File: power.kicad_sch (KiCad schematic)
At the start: 0 parts

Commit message: finish
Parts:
- added C26: 1uF, symbol G-Love:C
- added C27: 100nF, symbol G-Love:C
- added R16: 10K, symbol G-Love:R
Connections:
- new net +5V: C26.1, C27.1, R16.2
- new net GND: C26.2, C27.2, R16.1

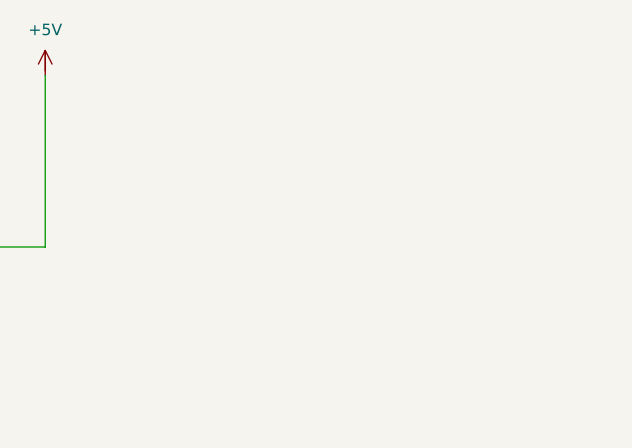
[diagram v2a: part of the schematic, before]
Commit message: Je crois que j'ai fini, je fais l'erc demain en revoyant la logique des switch, notamment les selections avec transistors
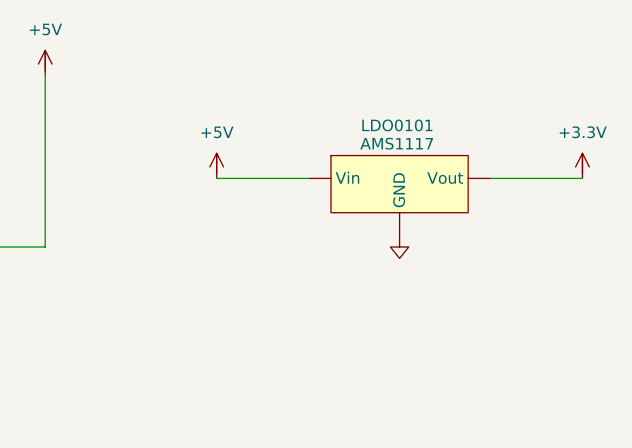
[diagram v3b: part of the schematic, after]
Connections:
- net GND is gone; now on net +5V: C26.2, C27.2, R16.1

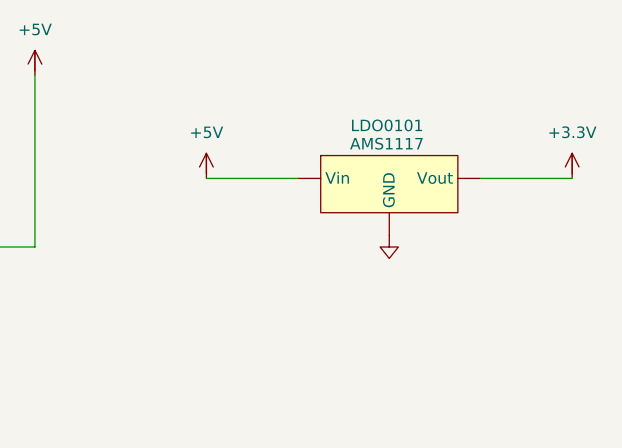
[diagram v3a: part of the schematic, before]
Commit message: To Do : Finir les condo pour chaque broche d'alimentation au moins avec ERC
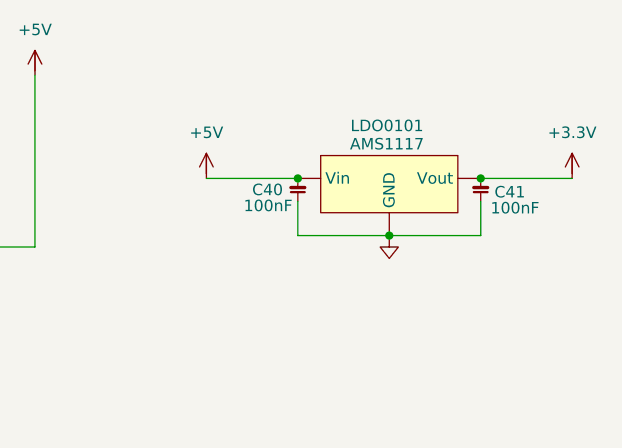
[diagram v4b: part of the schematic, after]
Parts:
- added C40, C41: 100nF, symbol G-Love:C
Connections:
- net +3.3V: now also C41.1
- net +5V: now also C40.1, C40.2, C41.2
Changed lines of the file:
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@@
+	)
+	(junction
+		(at 156.21 62.23)
+		(diameter 0)
+		(color 0 0 0 0)
+	)
+	(junction
+		(at 146.05 55.88)
+		(diameter 0)
+		(color 0 0 0 0)
+	)
+	(junction
+		(at 166.37 55.88)
+		(diameter 0)
+		(color 0 0 0 0)
 	)
 	(junction
@@
 	(wire
 		(pts
-			(xy 176.53 55.88) (xy 166.37 55.88)
+			(xy 146.05 62.23) (xy 156.21 62.23)
+		)
+		(stroke
+			(width 0)
+			(type default)
+		)
+	)
+	(wire
+		(pts
+			(xy 166.37 58.42) (xy 166.37 62.23)
 		)
 		(stroke
@@
 	(wire
 		(pts
+			(xy 166.37 55.88) (xy 176.53 55.88)
+		)
+		(stroke
+			(width 0)
+			(type default)
+		)
+	)
+	(wire
+		(pts
+			(xy 166.37 62.23) (xy 156.21 62.23)
+		)
+		(stroke
+			(width 0)
+			(type default)
+		)
+	)
+	(wire
+		(pts
 			(xy 67.31 63.5) (xy 76.2 63.5)
+		)
+		(stroke
+			(width 0)
+			(type default)
+		)
+	)
+	(wire
+		(pts
+			(xy 146.05 58.42) (xy 146.05 62.23)
 		)
 		(stroke
@@
 	(symbol
 		(lib_id "G-Love:C")
+		(at 146.05 57.15 0)
+		(unit 1)
+		(body_style 1)
+		(exclude_from_sim no)
+		(in_bom yes)
+		(on_board yes)
+		(in_pos_files yes)
+		(dnp no)
+		(property "Reference" "C40"
+			(at 140.97 57.15 0)
+			(show_name no)
+			(do_not_autoplace no)
+			(effects
+				(font
+					(size 1.27 1.27)
+				)
+				(justify left)
+			)
+		)
+		(property "Value" "100nF"
+			(at 142.748 58.928 0)
+			(show_name no)
+			(do_not_autoplace no)
+			(effects
+				(font
+					(size 1.27 1.27)
+				)
+			)
+		)
+		(property "Footprint" ""
+			(at 146.05 57.15 0)
+			(hide yes)
+			(show_name no)
+			(do_not_autoplace no)
+			(effects
+				(font
+					(size 1.27 1.27)
+				)
+			)
+		)
+		(property "Datasheet" ""
+			(at 146.05 57.15 0)
+			(hide yes)
+			(show_name no)
+			(do_not_autoplace no)
+			(effects
+				(font
+					(size 1.27 1.27)
+				)
+			)
+		)
+		(property "Description" "Capacitor"
+			(at 146.05 66.294 0)
+			(hide yes)
+			(show_name no)
+			(do_not_autoplace no)
+			(effects
+				(font
+					(size 1.27 1.27)
+				)
+			)
+		)
+		(pin "2"
+		)
+		(pin "1"
+		)
+		(instances
+			(project "G-Love"
+				(path "/808bc5ea-49ac-4454-ba77-8b20d01ce159/7d8a1e93-5494-4471-871c-2c3abe915f88"
+					(reference "C40")
+					(unit 1)
+				)
+			)
+		)
+	)
+	(symbol
+		(lib_id "G-Love:C")
 		(at 76.2 68.58 0)
 		(unit 1)
@@
 					(unit 1)
 				)
+			)
+		)
+	)
+	(symbol
+		(lib_id "G-Love:C")
+		(at 166.37 57.15 0)
+		(unit 1)
+		(body_style 1)
+		(exclude_from_sim no)
+		(in_bom yes)
+		(on_board yes)
+		(in_pos_files yes)
+		(dnp no)
+		(property "Reference" "C41"
+			(at 167.894 57.404 0)
+			(show_name no)
+			(do_not_autoplace no)
+			(effects
+				(font
+					(size 1.27 1.27)
+				)
+				(justify left)
+			)
+		)
+		(property "Value" "100nF"
+			(at 170.18 59.182 0)
+			(show_name no)
+			(do_not_autoplace no)
+			(effects
+				(font
+					(size 1.27 1.27)
+				)
+			)
+		)
+		(property "Footprint" ""
+			(at 166.37 57.15 0)
+			(hide yes)
+			(show_name no)
+			(do_not_autoplace no)
+			(effects
+				(font
+					(size 1.27 1.27)
+				)
+			)
+		)
+		(property "Datasheet" ""
+			(at 166.37 57.15 0)
+			(hide yes)
+			(show_name no)
+			(do_not_autoplace no)
+			(effects
+				(font
+					(size 1.27 1.27)
+				)
+			)
+		)
+		(property "Description" "Capacitor"
+			(at 166.37 66.294 0)
+			(hide yes)
+			(show_name no)
+			(do_not_autoplace no)
+			(effects
+				(font
+					(size 1.27 1.27)
+				)
+			)
+		)
+		(pin "1"
+		)
+		(pin "2"
+		)
+		(instances
+			(project "G-Love"
+				(path "/808bc5ea-49ac-4454-ba77-8b20d01ce159/7d8a1e93-5494-4471-871c-2c3abe915f88"
+					(reference "C41")
+					(unit 1)
+				)

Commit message: version final V1
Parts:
- added C29, C47: 1uF, symbol G-Love:C
- added C48: 4.7uF, symbol Device:C_Polarized_Small_US
- added C53: 10uF, symbol G-Love:C
- added R29: 560R, symbol G-Love:R
- added R32: 47k, symbol G-Love:R
- added R34: 10k, symbol G-Love:R
- added U14: TPS2113APWR, TPS2113APWR:SOP65P640X120-8N, symbol G-Love:TPS2113APWR
- renumbered C26 to C28, C27 to C31, C40 to C49, C41 to C50, R16 to R31
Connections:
- net +3.3V: now also C53.1
- net +5V: now also C29.1, C47.1, C48.1, C48.2, C53.2, R29.1, R34.1, U14.2 (~{EN}), U14.5 (GND), U14.7 (OUT)
- new net: R32.2, U14.3 (VSNS)
- new net: R29.2, U14.4 (ILIM)
- new net BATTERY_USB: C47.2, U14.6 (IN2)
- new net PC_USB: C29.2, R32.1, R34.2, U14.8 (IN1)
- no-connect marks 0 -> 1
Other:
- note added: "Alimentation LEDs"
- note added: "Alimentation PCB"
- note added: "LDO Sortie 3.3V"
- note added: "Pont diviseur de tension: si PC_USB < 4.3V, VSNS < 0.8V switch d'alim sur batterie Sinon utilisation USB"
- moved on the sheet: C28, C31, C49, C50, R31

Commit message: add: bom
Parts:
- C28, C29, C47: Price (none) -> 4.39/50; SUPPLIER (none) -> https://www.lcsc.com/product-detail/C15849.html
- C31, C49, C50: Price (none) -> 1.44/100; SUPPLIER (none) -> https://www.lcsc.com/product-detail/C1591.html
- C48: Price (none) -> 0.33/10; SUPPLIER (none) -> https://www.lcsc.com/product-detail/C19666.html
- C53: Price (none) -> 2.17/20; SUPPLIER (none) -> https://www.lcsc.com/product-detail/C15850.html
- R29: Price (none) -> 0.63/100; SUPPLIER (none) -> https://www.lcsc.com/product-detail/C23204.html
- R31: value 10K -> 10kΩ; Price (none) -> 0.74/100; SUPPLIER (none) -> https://www.lcsc.com/product-detail/C844918.html
- R32: Price (none) -> 0.24/100; SUPPLIER (none) -> https://www.lcsc.com/product-detail/C2907042.html
- R34: value 10k -> 10kΩ; Price (none) -> 0.74/100; SUPPLIER (none) -> https://www.lcsc.com/product-detail/C844918.html
- U14: Price None -> 2.67; SUPPLIER (none) -> https://www.lcsc.com/product-detail/C130052.html

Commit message: finished all footprints + redid some symbols, ready for PCB
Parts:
- C28, C29, C31, C47, C49, C50, C53: footprint (none) -> G-Love:Capacitor_0603
- C48: footprint (none) -> G-Love:Capacitor_Electrolytic
- R29, R31, R32, R34: footprint (none) -> G-Love:Resistor_0603
- U14: footprint TPS2113APWR:SOP65P640X120-8N -> G-Love:TPS2113
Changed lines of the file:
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@@
 			)
 		)
-		(property "Footprint" ""
+		(property "Footprint" "G-Love:Capacitor_0603"
 			(at 53.34 64.77 0)
 			(hide yes)
@@
 			)
 		)
-		(property "Footprint" "TPS2113APWR:SOP65P640X120-8N"
+		(property "Footprint" "G-Love:TPS2113"
 			(at 69.85 158.75 0)
 			(hide yes)
@@
 			)
 		)
-		(property "Footprint" ""
+		(property "Footprint" "G-Love:Capacitor_0603"
 			(at 142.24 154.94 0)
 			(hide yes)
@@
 			)
 		)
-		(property "Footprint" ""
+		(property "Footprint" "G-Love:Capacitor_0603"
 			(at 50.8 163.83 0)
 			(hide yes)
@@
 			)
 		)
-		(property "Footprint" ""
+		(property "Footprint" "G-Love:Capacitor_Electrolytic"
 			(at 91.44 160.02 0)
 			(hide yes)
@@
 			)
 		)
-		(property "Footprint" ""
+		(property "Footprint" "G-Love:Resistor_0603"
 			(at 66.04 64.77 0)
 			(hide yes)
@@
 			)
 		)
-		(property "Footprint" ""
+		(property "Footprint" "G-Love:Resistor_0603"
 			(at 44.45 153.67 0)
 			(hide yes)
@@
 			)
 		)
-		(property "Footprint" ""
+		(property "Footprint" "G-Love:Capacitor_0603"
 			(at 120.65 157.48 0)
 			(hide yes)
@@
 			)
 		)
-		(property "Footprint" ""
+		(property "Footprint" "G-Love:Capacitor_0603"
 			(at 40.64 64.77 0)
 			(hide yes)
@@
 			)
 		)
-		(property "Footprint" ""
+		(property "Footprint" "G-Love:Resistor_0603"
 			(at 87.63 146.05 0)
 			(hide yes)
@@
 			)
 		)
-		(property "Footprint" ""
+		(property "Footprint" "G-Love:Capacitor_0603"
 			(at 48.26 163.83 0)
 			(hide yes)
@@
 			)
 		)
-		(property "Footprint" ""
+		(property "Footprint" "G-Love:Resistor_0603"
 			(at 130.81 153.67 0)
 			(hide yes)
@@
 			)
 		)
-		(property "Footprint" ""
+		(property "Footprint" "G-Love:Resistor_0603"
 			(at 90.17 146.05 0)
 			(hide yes)
@@
 			)
 		)
-		(property "Footprint" ""
+		(property "Footprint" "G-Love:Capacitor_0603"
 			(at 149.86 154.94 0)
 			(hide yes)
